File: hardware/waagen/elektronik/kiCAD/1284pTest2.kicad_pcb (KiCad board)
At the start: 2 copper layers, 49.8 x 115.6 mm, 48 parts, among them J1 AVR-ISP-6, J2 Conn_01x06, J3 Conn_02x05_Odd_Even, J4 Conn_01x03_Male, J5 Conn_01x03_Male, J6 Conn_01x08, J7 Conn_01x03_Male, J8 Conn_01x03_Male, U1 ATmega1284P-P, U2 MCP1700-3302E_TO92, U3 SN65HVD230, U4 MCP2515, U5 NAU7802SGI, U6 DS18B20, Y1 12MHz, Y2 8MHz

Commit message: fues added and small movements
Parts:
- added F1: Polyfuse 500mA, Resistor_SMD:R_1206_3216Metric_Pad1.30x1.75mm_HandSolder, B.Cu at (93.5, 58.4)
- moved C7 22.8 mm to (95.5, 66.0), turned to -90 degrees
- moved C3 5.45 mm to (78.5, 94.0), turned to 0 degrees
- moved R10 1.78 mm to (105.4, 106.2)
- moved R4 1.78 mm to (105.4, 94.5), turned to -90 degrees
- moved U6 1.78 mm to (113.0, 104.9)
- moved C13 1.44 mm to (84.3, 145.3), turned to 180 degrees
- turned C8 to -90 degrees
- turned R3 to 90 degrees
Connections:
- C7 pad 1: +9V -> Net-(C7-Pad1)
- U2 pad 2: +9V -> Net-(C7-Pad1)
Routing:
- net +9V: track 27.9 -> 15.9 mm
- net Net-(C7-Pad1): track 0.00 -> 10.1 mm
- net Net-(C3-Pad1): track 3.52 -> 8.36 mm
- net /controller/RESET: track 94.2 -> 90.2 mm
- net Net-(C13-Pad2): track 8.00 -> 11.0 mm
- net Net-(C8-Pad1): track 4.57 -> 6.78 mm
- net VCC: track 244.1 -> 242.2 mm
- net /controller/I2C_DATA: track 56.5 -> 58.2 mm
- net Net-(C13-Pad1): track 10.9 -> 9.53 mm
- net /controller/I2C_CLK: track 60.1 -> 61.3 mm
- net /controller/OneWire: track 12.7 -> 12.2 mm
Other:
- board text added: "A K"
- board text added: "Scale Mainboard version 20. Feb 2022"
- board text removed: "Scale Mainboard version 19. Feb 2022"

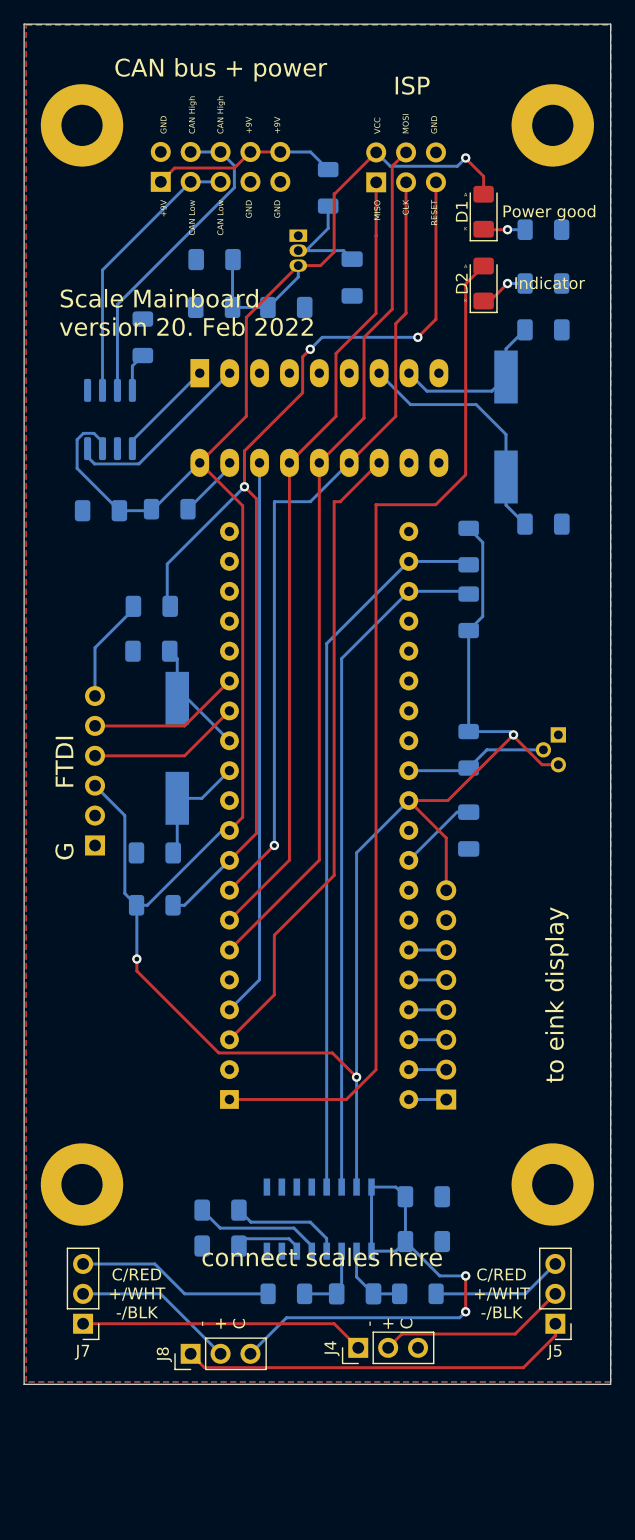
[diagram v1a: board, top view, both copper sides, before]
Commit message: CAN SPI CS pin corrected and PCB optimisations.
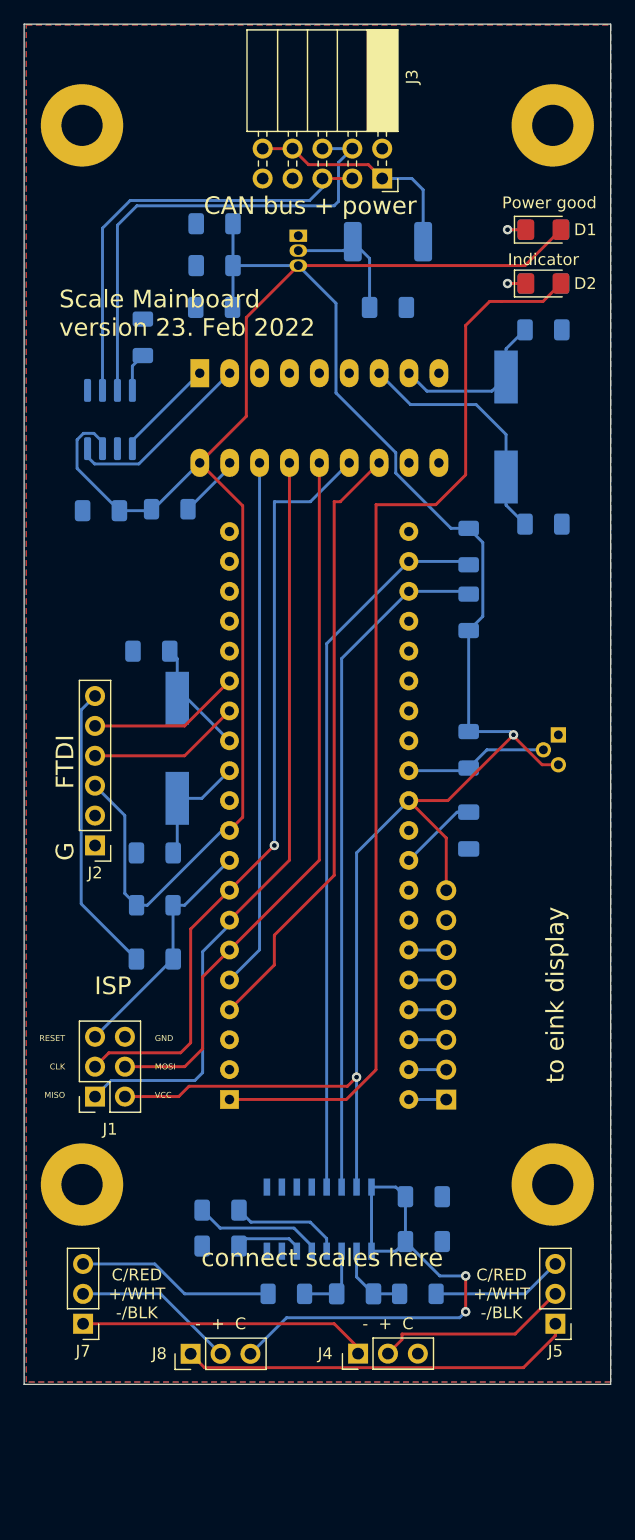
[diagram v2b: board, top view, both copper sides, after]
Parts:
- F1: value Polyfuse 500mA -> Fuse/Polyfuse 500mA; footprint Resistor_SMD:R_1206_3216Metric_Pad1.30x1.75mm_HandSolder -> Fuse:Fuse_2512_6332Metric_Pad1.52x3.35mm_HandSolder
- J1: footprint Connector_PinSocket_2.54mm:PinSocket_2x03_P2.54mm_Horizontal -> Connector_PinSocket_2.54mm:PinSocket_2x03_P2.54mm_Vertical; moved to F.Cu
- J2, J3: moved to F.Cu
- moved J1 81.3 mm to (73.7, 135.6), turned to 180 degrees
- moved C3 30.0 mm to (78.7, 124.0)
- moved J3 18.8 mm to (98.1, 57.6)
- moved C6 9.37 mm to (83.8, 61.5), turned to 180 degrees
- moved F1 6.83 mm to (98.6, 63.0), turned to 180 degrees
- moved D1 5.30 mm to (111.8, 62.0), turned to 0 degrees
- moved D2 5.08 mm to (111.8, 66.5), turned to 0 degrees
- moved C7 3.97 mm to (98.6, 68.6), turned to 0 degrees
- moved C5 0.51 mm to (83.8, 65.0)
- moved J4 0.49 mm to (96.0, 157.5)
- turned J2 to 180 degrees
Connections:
- U1 pad 3: /CAN/CAN_INT -> unconnected-(U1-Pad3)
- U1 pad 4: /CAN/CAN_CS -> /CAN/CAN_INT
- U1 pad 5: unconnected-(U1-Pad5) -> /CAN/CAN_CS
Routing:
- net /controller/RESET: track 90.2 -> 20.3 mm, vias 3 -> 0
- net VCC: track 242.2 -> 262.7 mm, vias 4 -> 2
- net Net-(C3-Pad1): track 8.36 -> 24.8 mm
- net /CAN_L: track 23.4 -> 37.2 mm
- net /CAN_H: track 27.4 -> 41.2 mm
- net /CAN/MOSI: track 74.0 -> 61.1 mm
- net Net-(D2-Pad2): track 88.6 -> 92.4 mm
- net +9V: track 15.9 -> 19.5 mm
- net /CAN/MISO: track 67.9 -> 64.9 mm
- net /CAN/SPI_CLK: track 68.2 -> 65.6 mm
- net /CAN/CAN_INT: track 54.6 -> 52.0 mm
- net /CAN/CAN_CS: track 47.5 -> 45.0 mm
- net Net-(D2-Pad1): track 4.15 -> 3.06 mm
- net Net-(C7-Pad1): track 10.1 -> 11.1 mm
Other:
- board text added: "+9V Low Low GND GND"
- board text added: "C + -"
- board text added: "GND MOSI VCC"
- board text added: "RESET CLK MISO"
- board text added: "Scale Mainboard version 23. Feb 2022"
- board text removed: "+9V CAN Low CAN Low GND GND"
- board text removed: "A K"
- board text removed: "MISO CLK RESET"
- board text removed: "Scale Mainboard version 20. Feb 2022"
- board text removed: "VCC MOSI GND"

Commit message: second LDO for eink added
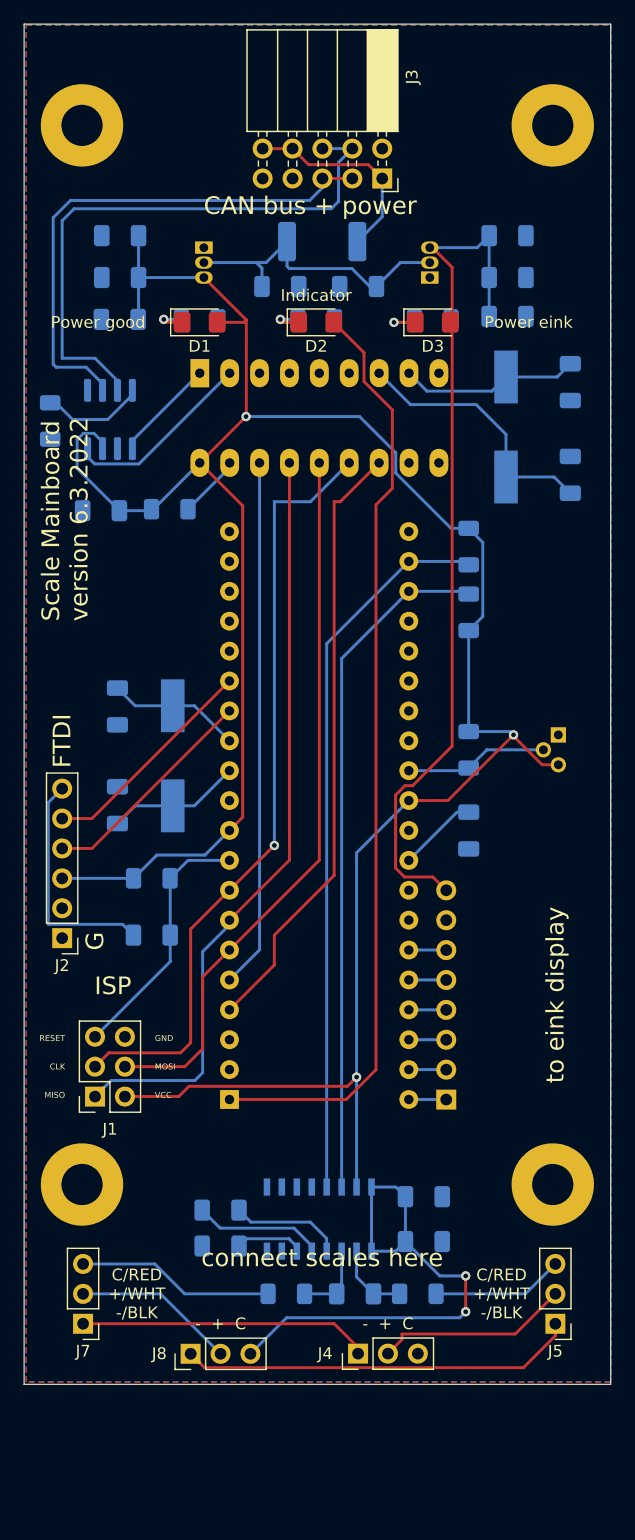
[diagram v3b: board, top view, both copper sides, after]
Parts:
- added C17: 100n, Capacitor_SMD:C_1206_3216Metric_Pad1.33x1.80mm_HandSolder, B.Cu at (108.7, 69.3)
- added C18: 10µ, Capacitor_SMD:C_1206_3216Metric_Pad1.33x1.80mm_HandSolder, B.Cu at (108.7, 66.0)
- added C19: 1µ, Capacitor_SMD:C_1206_3216Metric_Pad1.33x1.80mm_HandSolder, B.Cu at (108.7, 62.5)
- added C20: 1µ, Capacitor_SMD:C_1206_3216Metric_Pad1.33x1.80mm_HandSolder, B.Cu at (96.0, 66.8)
- added D3: LED, LED_SMD:LED_1206_3216Metric_Pad1.42x1.75mm_HandSolder, F.Cu at (102.4, 69.8)
- added R11: 120, Resistor_SMD:R_1206_3216Metric_Pad1.30x1.75mm_HandSolder, B.Cu at (102.4, 69.6)
- added U7: MCP1700-3302E_TO92, Package_TO_SOT_THT:TO-92_Inline, B.Cu at (102.1, 66.0)
- moved D1 30.3 mm to (82.5, 69.8)
- moved R2 30.2 mm to (82.5, 69.6)
- moved D2 19.6 mm to (92.5, 69.8)
- moved R5 19.5 mm to (92.5, 69.6)
- moved R6 10.6 mm to (69.8, 78.2), turned to -90 degrees
- moved C7 9.32 mm to (89.4, 66.8)
- moved J2 8.36 mm to (70.9, 122.2)
- moved U2 8.09 mm to (82.9, 63.5)
- moved C4 8.09 mm to (75.8, 69.6)
- moved C5 8.09 mm to (75.8, 66.0)
- moved C6 8.09 mm to (75.8, 62.5)
- moved F1 5.59 mm to (93.0, 63.0)
- moved C1 5.51 mm to (75.6, 102.5), turned to 90 degrees
- moved C2 5.16 mm to (75.6, 110.9), turned to -90 degrees
- moved C10 5.00 mm to (114.0, 74.9), turned to 90 degrees
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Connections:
- J6 pad 8: VCC -> /power/3V3_EINK
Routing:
- net /power/3V3_EINK: track 0.00 -> 73.4 mm
- net VCC: track 262.7 -> 219.8 mm, vias 2 -> 3
- net Net-(C7-Pad1): track 11.1 -> 25.8 mm
- net Net-(D2-Pad2): track 92.4 -> 79.6 mm
- net /CAN_H: track 41.2 -> 49.7 mm
- net /CAN_L: track 37.2 -> 45.1 mm
- net Net-(J2-Pad4): track 13.0 -> 19.1 mm
- net Net-(J2-Pad5): track 13.0 -> 19.1 mm
- net Net-(R6-Pad1): track 3.33 -> 8.82 mm
- net Net-(C3-Pad1): track 24.8 -> 19.6 mm
- net Net-(D3-Pad1): track 0.00 -> 3.67 mm, vias 0 -> 1
- net +9V: track 19.5 -> 17.5 mm
- net /controller/RESET: track 20.3 -> 21.8 mm
- net Net-(C9-Pad2): track 21.2 -> 22.6 mm
- net Net-(C10-Pad2): track 14.0 -> 15.3 mm
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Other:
- board text added: "3V3"
- board text added: "Power eink"
- board text added: "Scale Mainboard version 6.3.2022"
- board text removed: "Scale Mainboard version 23. Feb 2022"
- board text removed: "VCC"

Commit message: JP1 added
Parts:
- added JP1: SolderJumper_2_Open, Jumper:SolderJumper-2_P1.3mm_Open_RoundedPad1.0x1.5mm, B.Cu at (111.0, 113.0)
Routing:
- net /power/3V3_EINK: track 73.4 -> 82.7 mm
- net VCC: track 219.8 -> 225.5 mm
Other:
- board text added: "Scale Mainboard version 7.3.2022"
- board text removed: "Scale Mainboard version 6.3.2022"

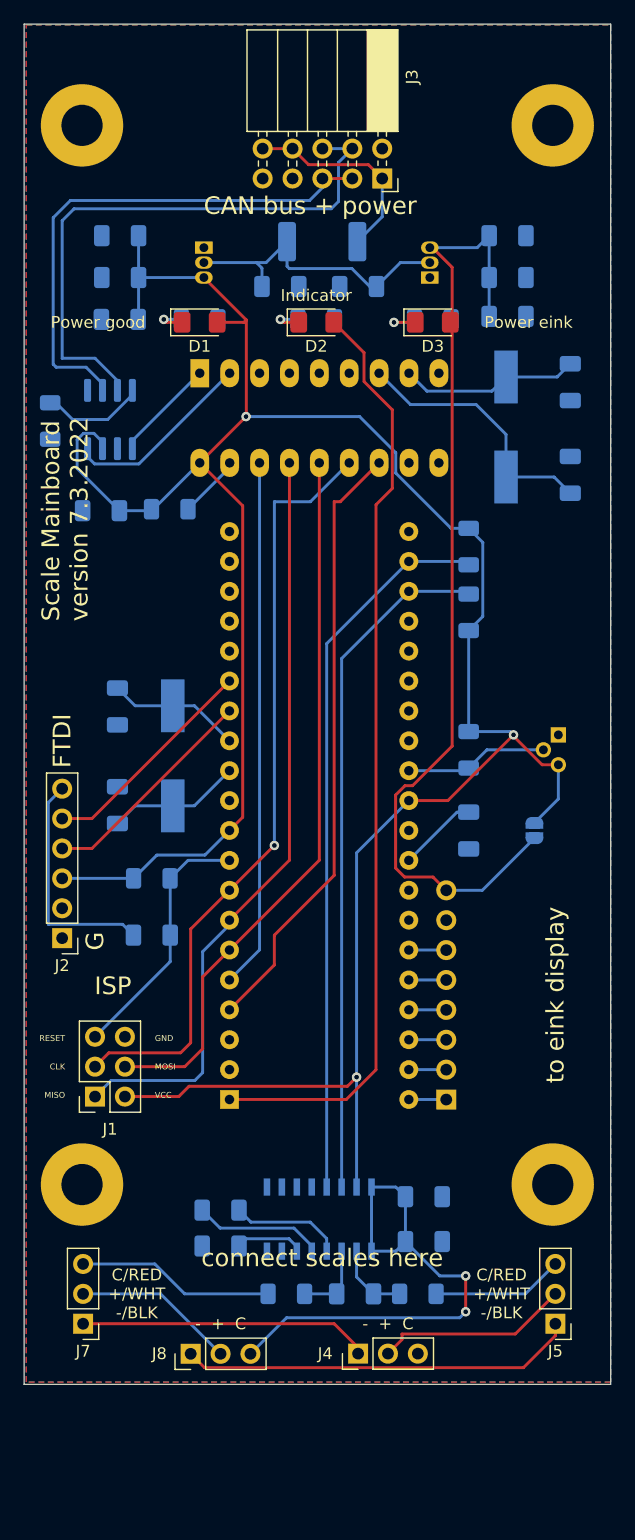
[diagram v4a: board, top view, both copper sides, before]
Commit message: Error on JP1 fixed and changed scale wires pads
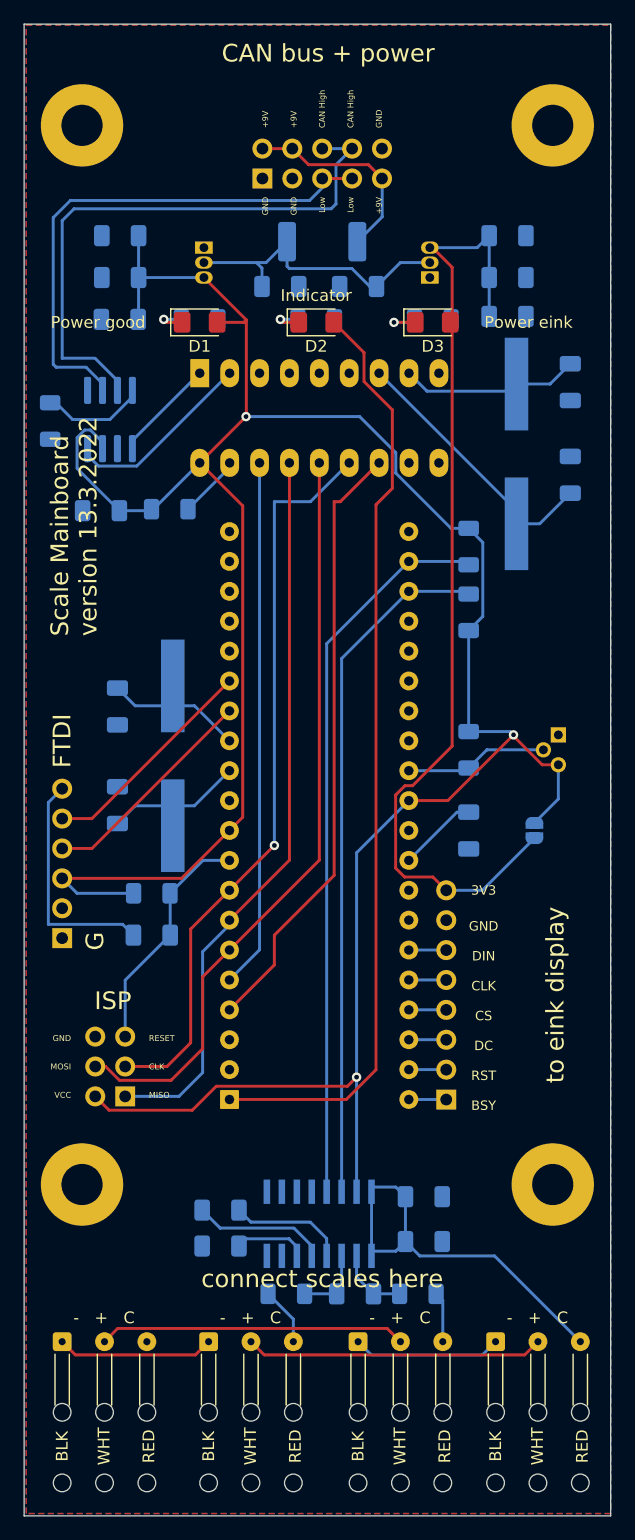
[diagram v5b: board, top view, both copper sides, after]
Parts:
- J1, J3: moved to B.Cu
- J2: footprint Connector_PinHeader_2.54mm:PinHeader_1x06_P2.54mm_Vertical -> Connector_PinSocket_2.54mm:PinSocket_1x06_P2.54mm_Vertical; moved to B.Cu
- J4, J5, J7, J8: footprint Connector_PinHeader_2.54mm:PinHeader_1x03_P2.54mm_Vertical -> Connector_Wire:SolderWire-0.1sqmm_1x03_P3.6mm_D0.4mm_OD1mm_Relief2x
- Y1, Y2: footprint Crystal:Crystal_SMD_HC49-SD -> Crystal:Crystal_SMD_HC49-SD_HandSoldering
- moved J8 25.9 mm to (107.7, 156.5), turned to 0 degrees
- moved J4 25.2 mm to (70.9, 156.5), turned to 0 degrees
- moved J5 16.8 mm to (96.0, 156.5), turned to 0 degrees
- moved J7 10.8 mm to (83.3, 156.5), turned to 0 degrees
- moved J3 10.2 mm to (87.9, 57.6)
- moved J1 2.56 mm to (76.2, 135.6), turned to 0 degrees
- moved Y2 2.45 mm to (109.5, 81.0)
- moved R1 1.27 mm to (78.5, 118.4)
- moved U5 0.40 mm to (92.7, 146.4)
- turned J2 to 0 degrees
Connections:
- J3 pad 1: +9V -> GND
- J3 pad 10: +9V -> GND
- J3 pad 2: GND -> +9V
- J3 pad 3: /CAN_L -> GND
- J3 pad 4: /CAN_H -> +9V
- J3 pad 7: GND -> /CAN_L
- J3 pad 8: +9V -> /CAN_H
- J3 pad 9: GND -> +9V
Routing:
- net Net-(J5-Pad1): track 33.6 -> 12.6 mm
- net Net-(J7-Pad3): track 16.8 -> 4.95 mm
- net Net-(J7-Pad2): track 13.8 -> 25.3 mm
- net Net-(J4-Pad1): track 24.7 -> 13.4 mm
- net VCC: track 225.5 -> 236.5 mm
- net /scale/NAU_VDDA: track 44.8 -> 34.1 mm, vias 2 -> 0
- net Net-(J4-Pad2): track 16.6 -> 26.1 mm
- net Net-(J5-Pad3): track 11.2 -> 4.30 mm
- net /CAN/MOSI: track 61.1 -> 64.6 mm
- net /CAN/SPI_CLK: track 65.6 -> 63.1 mm
- net /CAN/MISO: track 64.9 -> 62.3 mm
- net /controller/RESET: track 21.8 -> 20.0 mm
- net Net-(C9-Pad2): track 22.6 -> 23.3 mm
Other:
- board size 49.8 x 115.6 mm -> 49.8 x 126.8 mm
- board text added: "+9V +9V CAN High CAN High GND"
- board text added: "BLK"
- board text added: "GND GND Low Low +9V"
- board text added: "RED"
- board text added: "Scale Mainboard version 13.3.2022"
- board text added: "WHT"
- board text removed: "+9V Low Low GND GND"
- board text removed: "C/RED +/WHT -/BLK"
- board text removed: "GND CAN High CAN High +9V +9V"
- board text removed: "Scale Mainboard version 7.3.2022"

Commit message: bus terminator and shelf controller added
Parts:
- J1: footprint Connector_PinSocket_2.54mm:PinSocket_2x03_P2.54mm_Vertical -> Connector_PinHeader_2.54mm:PinHeader_2x03_P2.54mm_Vertical
- moved J1 2.56 mm to (73.7, 135.6)
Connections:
- J1 pad 2: VCC -> +9V
- J2 pad 3: VCC -> +9V
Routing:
- net +9V: track 17.5 -> 118.2 mm
- net VCC: track 236.5 -> 200.7 mm, vias 3 -> 2
- net /CAN/MISO: track 62.3 -> 65.8 mm
- net /CAN/MOSI: track 64.6 -> 61.1 mm
- net /CAN/SPI_CLK: track 63.1 -> 65.6 mm
- net /controller/RESET: track 20.0 -> 21.0 mm
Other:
- board text added: "GND MOSI +9V"
- board text removed: "GND MOSI VCC"
